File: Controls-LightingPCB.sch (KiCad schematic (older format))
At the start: 9 parts, among them J1 MinionConn, J3 Gecko_Cable, U1 LTC6820, U2 HX1188FNL

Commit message: Switched LEDs to back side and changed dimensions of board
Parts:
- removed J3: Gecko_Cable, UTSVT_Connectors:ribbon_cable_right_2x10, symbol Connector_Generic:Conn_02x10_Counter_Clockwise
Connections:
- net labels removed: UART-Tx, UART_Rx
- wire segments 77 -> 71
- no-connect marks 28 -> 14
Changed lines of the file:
@@
 Text Label 4350 4600 0    50   ~ 0
 IM
-Text Label 7150 4350 2    50   ~ 0
-UART-Tx
-Text Label 7150 4450 2    50   ~ 0
-UART_Rx
 $Sheet
 S 1750 1500 650  800
@@
 Wire Wire Line
 	2400 2200 2800 2200
-$Comp
-L Connector_Generic:Conn_02x10_Counter_Clockwise J3
-U 1 1 5F87CE03
-P 7800 4350
-F 0 "J3" H 7850 3625 50  0000 C CNN
-F 1 "Gecko_Cable" H 7850 3716 50  0000 C CNN
-F 2 "UTSVT_Connectors:ribbon_cable_right_2x10" H 7800 4350 50  0001 C CNN
-F 3 "~" H 7800 4350 50  0001 C CNN
-	1    7800 4350
-	-1   0    0    1
-$EndComp
-NoConn ~ 7500 3950
-NoConn ~ 7500 4050
-NoConn ~ 7500 4150
-NoConn ~ 7500 4250
-NoConn ~ 7500 4550
-NoConn ~ 7500 4650
-NoConn ~ 7500 4750
-NoConn ~ 8000 4650
-NoConn ~ 8000 4550
-NoConn ~ 8000 4450
-NoConn ~ 8000 4350
-NoConn ~ 8000 4250
-NoConn ~ 8000 4150
-NoConn ~ 8000 4050
-NoConn ~ 8000 3950
-NoConn ~ 8000 3850
-Wire Wire Line
-	7500 4450 6800 4450
-Wire Wire Line
-	6800 4350 7500 4350
-$Comp
-L power:GND #PWR0112
-U 1 1 5F8A761E
-P 8200 4850
-F 0 "#PWR0112" H 8200 4600 50  0001 C CNN
-F 1 "GND" H 8205 4677 50  0000 C CNN
-F 2 "" H 8200 4850 50  0001 C CNN
-F 3 "" H 8200 4850 50  0001 C CNN
-	1    8200 4850
-	-1   0    0    -1
-$EndComp
-$Comp
-L power:+3.3V #PWR0113
-U 1 1 5F8A7AF6
-P 7300 3750
-F 0 "#PWR0113" H 7300 3600 50  0001 C CNN
-F 1 "+3.3V" H 7315 3923 50  0000 C CNN
-F 2 "" H 7300 3750 50  0001 C CNN
-F 3 "" H 7300 3750 50  0001 C CNN
-	1    7300 3750
-	-1   0    0    -1
-$EndComp
-Wire Wire Line
-	7300 3750 7300 3850
-Wire Wire Line
-	7300 3850 7500 3850
-Wire Wire Line
-	8000 4750 8200 4750
-Wire Wire Line
-	8200 4750 8200 4850
 Wire Wire Line
 	6000 3350 6000 3450
@@
 Wire Wire Line
 	6000 3450 6100 3450
+NoConn ~ 6800 4350
+NoConn ~ 6800 4450
 $EndSCHEMATC

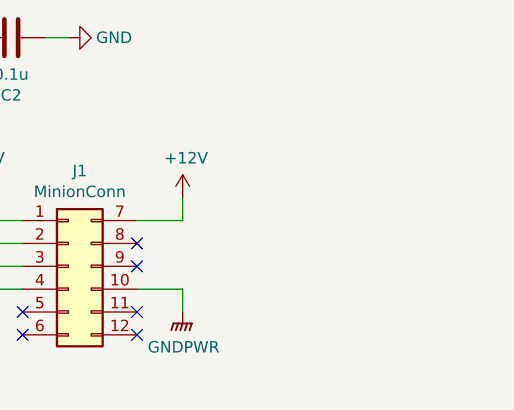
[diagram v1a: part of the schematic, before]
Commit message: Added mounting holes and adjusted design accordingly
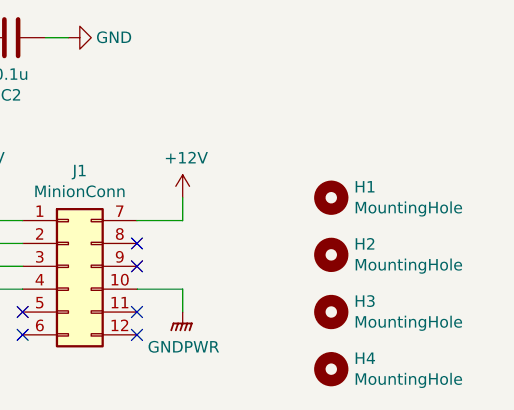
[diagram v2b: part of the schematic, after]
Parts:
- added H1, H2, H3, H4: MountingHole, MountingHole:MountingHole_3mm, symbol Mechanical:MountingHole
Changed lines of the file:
@@
 NoConn ~ 6800 4350
 NoConn ~ 6800 4450
+$Comp
+L Mechanical:MountingHole H4
+U 1 1 5F95A591
+P 7650 4900
+F 0 "H4" H 7750 4946 50  0000 L CNN
+F 1 "MountingHole" H 7750 4855 50  0000 L CNN
+F 2 "MountingHole:MountingHole_3mm" H 7650 4900 50  0001 C CNN
+F 3 "~" H 7650 4900 50  0001 C CNN
+	1    7650 4900
+	1    0    0    -1
+$EndComp
+$Comp
+L Mechanical:MountingHole H3
+U 1 1 5F95AB20
+P 7650 4650
+F 0 "H3" H 7750 4696 50  0000 L CNN
+F 1 "MountingHole" H 7750 4605 50  0000 L CNN
+F 2 "MountingHole:MountingHole_3mm" H 7650 4650 50  0001 C CNN
+F 3 "~" H 7650 4650 50  0001 C CNN
+	1    7650 4650
+	1    0    0    -1
+$EndComp
+$Comp
+L Mechanical:MountingHole H2
+U 1 1 5F95AF4E
+P 7650 4400
+F 0 "H2" H 7750 4446 50  0000 L CNN
+F 1 "MountingHole" H 7750 4355 50  0000 L CNN
+F 2 "MountingHole:MountingHole_3mm" H 7650 4400 50  0001 C CNN
+F 3 "~" H 7650 4400 50  0001 C CNN
+	1    7650 4400
+	1    0    0    -1
+$EndComp
+$Comp
+L Mechanical:MountingHole H1
+U 1 1 5F95B613
+P 7650 4150
+F 0 "H1" H 7750 4196 50  0000 L CNN
+F 1 "MountingHole" H 7750 4105 50  0000 L CNN
+F 2 "MountingHole:MountingHole_3mm" H 7650 4150 50  0001 C CNN
+F 3 "~" H 7650 4150 50  0001 C CNN
+	1    7650 4150
+	1    0    0    -1
+$EndComp
 $EndSCHEMATC

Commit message: Minor changes
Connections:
- net +3V3: no longer J1.1 (Pin_1)
- net GND: no longer J1.4 (Pin_4)
- no-connect marks 14 -> 16
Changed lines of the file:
@@
 $Descr A4 11693 8268
 encoding utf-8
-Sheet 1 4
+Sheet 1 5
 Title ""
 Date ""
@@
 $EndSheet
 Wire Wire Line
-	6100 4250 6300 4250
-Wire Wire Line
-	6100 4150 6100 4250
-Wire Wire Line
-	6100 4550 6300 4550
-Wire Wire Line
-	6100 4650 6100 4550
-$Comp
-L power:GND #PWR0101
-U 1 1 5F7E37DD
-P 6100 4650
-F 0 "#PWR0101" H 6100 4400 50  0001 C CNN
-F 1 "GND" H 6105 4477 50  0000 C CNN
-F 2 "" H 6100 4650 50  0001 C CNN
-F 3 "" H 6100 4650 50  0001 C CNN
-	1    6100 4650
-	1    0    0    -1
-$EndComp
-$Comp
-L power:+3.3V #PWR0102
-U 1 1 5F7E3562
-P 6100 4150
-F 0 "#PWR0102" H 6100 4000 50  0001 C CNN
-F 1 "+3.3V" H 6115 4323 50  0000 C CNN
-F 2 "" H 6100 4150 50  0001 C CNN
-F 3 "" H 6100 4150 50  0001 C CNN
-	1    6100 4150
-	1    0    0    -1
-$EndComp
-Wire Wire Line
 	7000 4250 7000 4150
 Wire Wire Line
@@
 	1    0    0    -1
 $EndComp
+$Comp
+L power:GND #PWR01
+U 1 1 5FA7B897
+P 3550 4250
+F 0 "#PWR01" H 3550 4000 50  0001 C CNN
+F 1 "GND" H 3555 4077 50  0000 C CNN
+F 2 "" H 3550 4250 50  0001 C CNN
+F 3 "" H 3550 4250 50  0001 C CNN
+	1    3550 4250
+	1    0    0    -1
+$EndComp
+NoConn ~ 6300 4550
+NoConn ~ 6300 4250
+$Sheet
+S 2700 3650 550  600
+U 5FA72DEA
+F0 "PowerDist" 50
+F1 "PowerDist.sch" 50
+F2 "GND" O R 3250 4150 50
+F3 "+5V" O R 3250 3850 50
+F4 "+3.3V" I R 3250 3950 50
+F5 "+12V" I R 3250 3750 50
+F6 "GNDPWR" I R 3250 4050 50
+$EndSheet
+$Comp
+L power:GNDPWR #PWR?
+U 1 1 5FA815F4
+P 3850 4250
+F 0 "#PWR?" H 3850 4050 50  0001 C CNN
+F 1 "GNDPWR" H 3854 4096 50  0000 C CNN
+F 2 "" H 3850 4200 50  0001 C CNN
+F 3 "" H 3850 4200 50  0001 C CNN
+	1    3850 4250
+	1    0    0    -1
+$EndComp
+$Comp
+L power:+3.3V #PWR?
+U 1 1 5FA8203D
+P 3900 3650
+F 0 "#PWR?" H 3900 3500 50  0001 C CNN
+F 1 "+3.3V" H 3915 3823 50  0000 C CNN
+F 2 "" H 3900 3650 50  0001 C CNN
+F 3 "" H 3900 3650 50  0001 C CNN
+	1    3900 3650
+	1    0    0    -1
+$EndComp
+$Comp
+L power:+5V #PWR?
+U 1 1 5FA82F89
+P 3700 3650
+F 0 "#PWR?" H 3700 3500 50  0001 C CNN
+F 1 "+5V" H 3715 3823 50  0000 C CNN
+F 2 "" H 3700 3650 50  0001 C CNN
+F 3 "" H 3700 3650 50  0001 C CNN
+	1    3700 3650
+	1    0    0    -1
+$EndComp
+$Comp
+L power:+12V #PWR?
+U 1 1 5FA838E6
+P 3500 3650
+F 0 "#PWR?" H 3500 3500 50  0001 C CNN
+F 1 "+12V" H 3515 3823 50  0000 C CNN
+F 2 "" H 3500 3650 50  0001 C CNN
+F 3 "" H 3500 3650 50  0001 C CNN
+	1    3500 3650
+	1    0    0    -1
+$EndComp
+Wire Wire Line
+	3250 4150 3550 4150
+Wire Wire Line
+	3550 4150 3550 4250
+Wire Wire Line
+	3250 4050 3850 4050
+Wire Wire Line
+	3850 4050 3850 4250
+Wire Wire Line
+	3250 3950 3900 3950
+Wire Wire Line
+	3900 3950 3900 3650
+Wire Wire Line
+	3250 3850 3700 3850
+Wire Wire Line
+	3700 3850 3700 3650
+Wire Wire Line
+	3250 3750 3500 3750
+Wire Wire Line
+	3500 3750 3500 3650
 $EndSCHEMATC

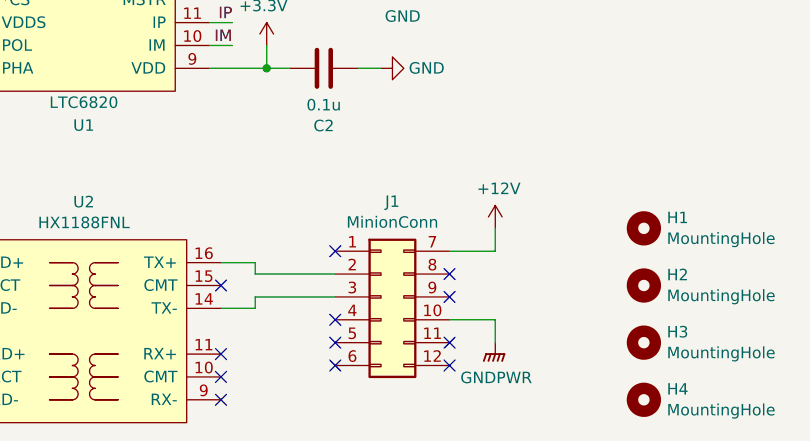
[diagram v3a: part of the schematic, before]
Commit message: Changed all switch connectors to horizontal, board dimensions to 2.5in by 4.5in, and started board layout
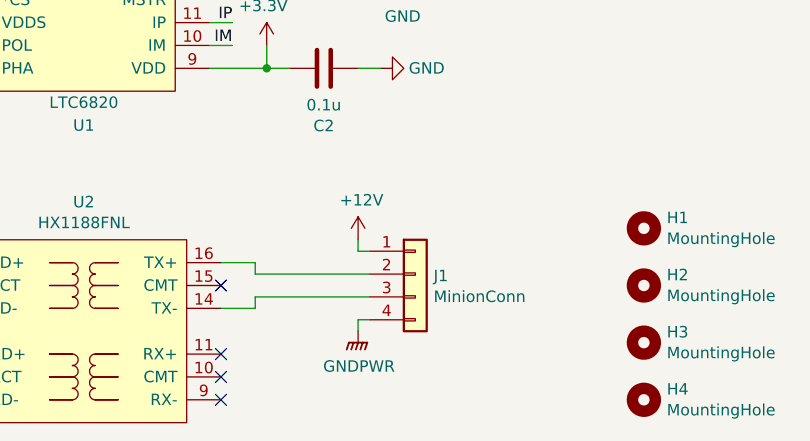
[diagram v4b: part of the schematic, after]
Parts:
- removed J1: MinionConn, UTSVT_Connectors:Molex_MicroFit3.0_2x6xP3.00mm_PolarizingPeg_Vertical, symbol Connector_Generic:Conn_02x06_Top_Bottom
- added J1: MinionConn, Connector_Molex:Molex_Micro-Fit_3.0_43650-0400_1x04_P3.00mm_Horizontal, symbol Connector_Generic:Conn_01x04
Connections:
- net +12V: now also J1.1 (Pin_1)
- net GNDPWR: now also J1.4 (Pin_4)
- net at U2.16 (TX+): now also J1.2 (Pin_2)
- net at U2.14 (TX-): now also J1.3 (Pin_3)
- no-connect marks 16 -> 8
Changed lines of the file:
@@
 F21 "MOSI" O R 4050 2850 50
 $EndSheet
-Wire Wire Line
-	7000 4250 7000 4150
-Wire Wire Line
-	6800 4250 7000 4250
-Wire Wire Line
-	7000 4550 7000 4650
-Wire Wire Line
-	6800 4550 7000 4550
-NoConn ~ 6300 4750
-NoConn ~ 6300 4650
-NoConn ~ 6800 4750
-NoConn ~ 6800 4650
 $Comp
 L power:GNDPWR #PWR0103
 U 1 1 5F7E16B8
-P 7000 4650
-F 0 "#PWR0103" H 7000 4450 50  0001 C CNN
-F 1 "GNDPWR" H 7004 4496 50  0000 C CNN
-F 2 "" H 7000 4600 50  0001 C CNN
-F 3 "" H 7000 4600 50  0001 C CNN
-	1    7000 4650
+P 6400 4600
+F 0 "#PWR0103" H 6400 4400 50  0001 C CNN
+F 1 "GNDPWR" H 6404 4446 50  0000 C CNN
+F 2 "" H 6400 4550 50  0001 C CNN
+F 3 "" H 6400 4550 50  0001 C CNN
+	1    6400 4600
 	1    0    0    -1
 $EndComp
@@
 L power:+12V #PWR0104
 U 1 1 5F7E142C
-P 7000 4150
-F 0 "#PWR0104" H 7000 4000 50  0001 C CNN
-F 1 "+12V" H 7015 4323 50  0000 C CNN
-F 2 "" H 7000 4150 50  0001 C CNN
-F 3 "" H 7000 4150 50  0001 C CNN
-	1    7000 4150
-	1    0    0    -1
-$EndComp
-$Comp
-L Connector_Generic:Conn_02x06_Top_Bottom J1
-U 1 1 5F7DD986
-P 6500 4450
-F 0 "J1" H 6550 4867 50  0000 C CNN
-F 1 "MinionConn" H 6550 4776 50  0000 C CNN
-F 2 "UTSVT_Connectors:Molex_MicroFit3.0_2x6xP3.00mm_PolarizingPeg_Vertical" H 6500 4450 50  0001 C CNN
-F 3 "~" H 6500 4450 50  0001 C CNN
-	1    6500 4450
+P 6400 4200
+F 0 "#PWR0104" H 6400 4050 50  0001 C CNN
+F 1 "+12V" H 6415 4373 50  0000 C CNN
+F 2 "" H 6400 4200 50  0001 C CNN
+F 3 "" H 6400 4200 50  0001 C CNN
+	1    6400 4200
 	1    0    0    -1
 $EndComp
@@
 	5950 4300 5950 4350
 Wire Wire Line
-	5950 4350 6300 4350
-Wire Wire Line
 	5800 4500 5950 4500
 Wire Wire Line
 	5950 4500 5950 4450
-Wire Wire Line
-	5950 4450 6300 4450
 NoConn ~ 5800 4400
 NoConn ~ 5800 4700
@@
 Wire Wire Line
 	6000 3450 6100 3450
-NoConn ~ 6800 4350
-NoConn ~ 6800 4450
 $Comp
 L Mechanical:MountingHole H4
@@
 	1    0    0    -1
 $EndComp
-NoConn ~ 6300 4550
-NoConn ~ 6300 4250
 $Sheet
 S 2700 3650 550  600
@@
 $EndSheet
 $Comp
-L power:GNDPWR #PWR?
+L power:GNDPWR #PWR0101
 U 1 1 5FA815F4
 P 3850 4250
-F 0 "#PWR?" H 3850 4050 50  0001 C CNN
+F 0 "#PWR0101" H 3850 4050 50  0001 C CNN
 F 1 "GNDPWR" H 3854 4096 50  0000 C CNN
 F 2 "" H 3850 4200 50  0001 C CNN
@@
 $EndComp
 $Comp
-L power:+3.3V #PWR?
+L power:+3.3V #PWR0102
 U 1 1 5FA8203D
 P 3900 3650
-F 0 "#PWR?" H 3900 3500 50  0001 C CNN
+F 0 "#PWR0102" H 3900 3500 50  0001 C CNN
 F 1 "+3.3V" H 3915 3823 50  0000 C CNN
 F 2 "" H 3900 3650 50  0001 C CNN
@@
 $EndComp
 $Comp
-L power:+5V #PWR?
+L power:+5V #PWR0112
 U 1 1 5FA82F89
 P 3700 3650
-F 0 "#PWR?" H 3700 3500 50  0001 C CNN
+F 0 "#PWR0112" H 3700 3500 50  0001 C CNN
 F 1 "+5V" H 3715 3823 50  0000 C CNN
 F 2 "" H 3700 3650 50  0001 C CNN
@@
 $EndComp
 $Comp
-L power:+12V #PWR?
+L power:+12V #PWR0113
 U 1 1 5FA838E6
 P 3500 3650
-F 0 "#PWR?" H 3500 3500 50  0001 C CNN
+F 0 "#PWR0113" H 3500 3500 50  0001 C CNN
 F 1 "+12V" H 3515 3823 50  0000 C CNN
 F 2 "" H 3500 3650 50  0001 C CNN
@@
 Wire Wire Line
 	3500 3750 3500 3650
+$Comp
+L Connector_Generic:Conn_01x04 J1
+U 1 1 5FBD3314
+P 6650 4350
+F 0 "J1" H 6730 4342 50  0000 L CNN
+F 1 "MinionConn" H 6730 4251 50  0000 L CNN
+F 2 "Connector_Molex:Molex_Micro-Fit_3.0_43650-0400_1x04_P3.00mm_Horizontal" H 6650 4350 50  0001 C CNN
+F 3 "~" H 6650 4350 50  0001 C CNN
+	1    6650 4350
+	1    0    0    -1
+$EndComp
+Wire Wire Line
+	6400 4200 6400 4250
+Wire Wire Line
+	6400 4250 6450 4250
+Wire Wire Line
+	6450 4550 6400 4550
+Wire Wire Line
+	6400 4550 6400 4600
+Wire Wire Line
+	5950 4350 6450 4350
+Wire Wire Line
+	5950 4450 6450 4450
 $EndSCHEMATC

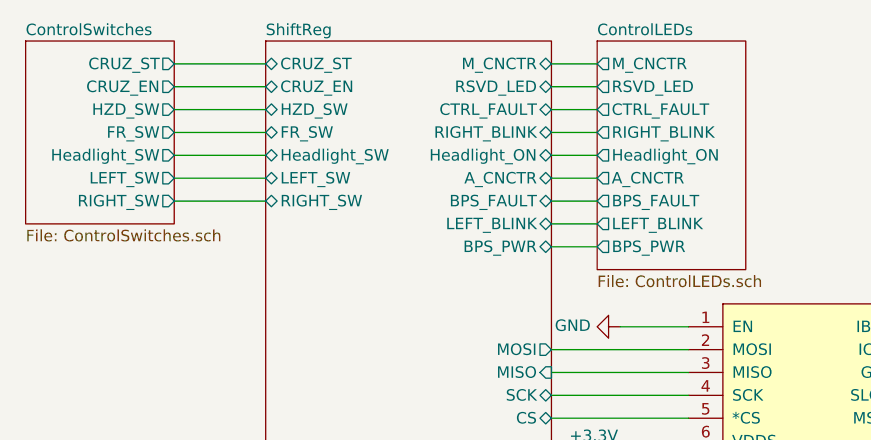
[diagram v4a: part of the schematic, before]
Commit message: Added Regen switch, deleted RSVD LED
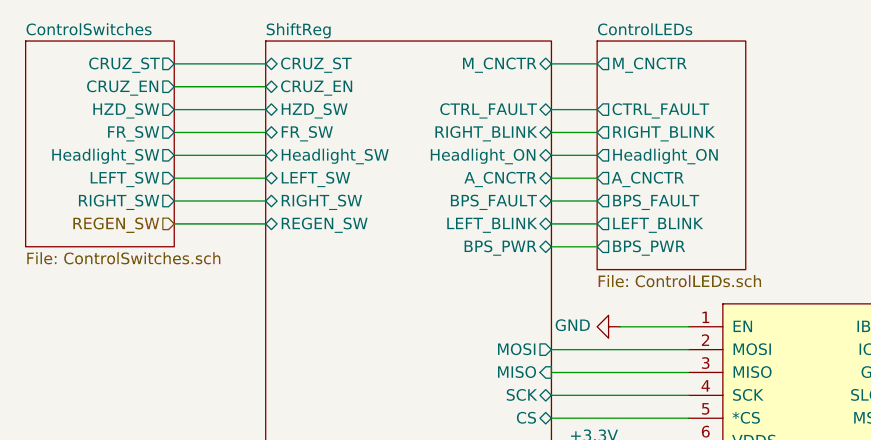
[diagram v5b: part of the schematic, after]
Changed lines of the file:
@@
 	4250 1800 4050 1800
-Wire Wire Line
-	4050 1700 4250 1700
 Wire Wire Line
 	4250 1600 4050 1600
@@
 F1 "ControlLEDs.sch" 50
 F2 "M_CNCTR" O L 4250 1600 50
-F3 "RSVD_LED" O L 4250 1700 50
-F4 "A_CNCTR" O L 4250 2100 50
-F5 "CTRL_FAULT" O L 4250 1800 50
-F6 "RIGHT_BLINK" O L 4250 1900 50
-F7 "Headlight_ON" O L 4250 2000 50
-F8 "BPS_FAULT" O L 4250 2200 50
-F9 "LEFT_BLINK" O L 4250 2300 50
-F10 "BPS_PWR" O L 4250 2400 50
+F3 "A_CNCTR" O L 4250 2100 50
+F4 "CTRL_FAULT" O L 4250 1800 50
+F5 "RIGHT_BLINK" O L 4250 1900 50
+F6 "Headlight_ON" O L 4250 2000 50
+F7 "BPS_FAULT" O L 4250 2200 50
+F8 "LEFT_BLINK" O L 4250 2300 50
+F9 "BPS_PWR" O L 4250 2400 50
 $EndSheet
 $Sheet
@@
 F1 "ShiftReg.sch" 50
 F2 "M_CNCTR" B R 4050 1600 50
-F3 "RSVD_LED" B R 4050 1700 50
-F4 "CTRL_FAULT" B R 4050 1800 50
-F5 "RIGHT_BLINK" B R 4050 1900 50
-F6 "Headlight_ON" B R 4050 2000 50
-F7 "A_CNCTR" B R 4050 2100 50
-F8 "BPS_FAULT" B R 4050 2200 50
-F9 "LEFT_BLINK" B R 4050 2300 50
-F10 "BPS_PWR" B R 4050 2400 50
-F11 "CRUZ_ST" B L 2800 1600 50
-F12 "CRUZ_EN" B L 2800 1700 50
-F13 "HZD_SW" B L 2800 1800 50
-F14 "FR_SW" B L 2800 1900 50
-F15 "Headlight_SW" B L 2800 2000 50
-F16 "LEFT_SW" B L 2800 2100 50
-F17 "RIGHT_SW" B L 2800 2200 50
-F18 "CS" B R 4050 3150 50
-F19 "SCK" B R 4050 3050 50
-F20 "MISO" I R 4050 2950 50
-F21 "MOSI" O R 4050 2850 50
+F3 "CTRL_FAULT" B R 4050 1800 50
+F4 "RIGHT_BLINK" B R 4050 1900 50
+F5 "Headlight_ON" B R 4050 2000 50
+F6 "A_CNCTR" B R 4050 2100 50
+F7 "BPS_FAULT" B R 4050 2200 50
+F8 "LEFT_BLINK" B R 4050 2300 50
+F9 "BPS_PWR" B R 4050 2400 50
+F10 "CRUZ_ST" B L 2800 1600 50
+F11 "CRUZ_EN" B L 2800 1700 50
+F12 "HZD_SW" B L 2800 1800 50
+F13 "FR_SW" B L 2800 1900 50
+F14 "Headlight_SW" B L 2800 2000 50
+F15 "LEFT_SW" B L 2800 2100 50
+F16 "RIGHT_SW" B L 2800 2200 50
+F17 "CS" B R 4050 3150 50
+F18 "SCK" B R 4050 3050 50
+F19 "MISO" I R 4050 2950 50
+F20 "MOSI" O R 4050 2850 50
+F21 "REGEN_SW" B L 2800 2300 50
 $EndSheet
 $Comp
@@
 IM
 $Sheet
-S 1750 1500 650  800
+S 1750 1500 650  900
 U 5F78B3EB
 F0 "ControlSwitches" 50
@@
 Wire Wire Line
 	5950 4450 6450 4450
+Text HLabel 2400 2300 0    50   Input ~ 0
+REGEN_SW
+Wire Wire Line
+	2400 2300 2800 2300
 $EndSCHEMATC

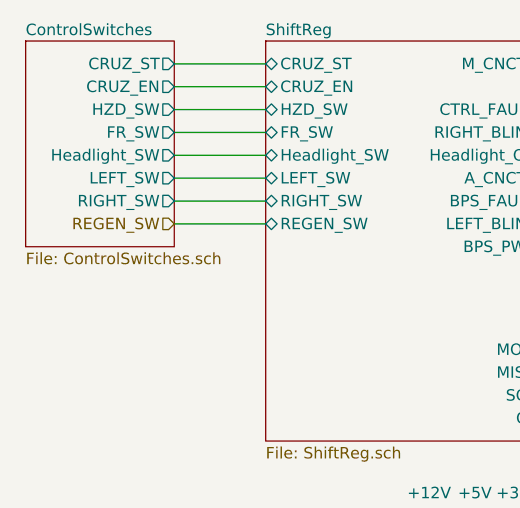
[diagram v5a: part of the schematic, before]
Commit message: Started placing routes, did not finish
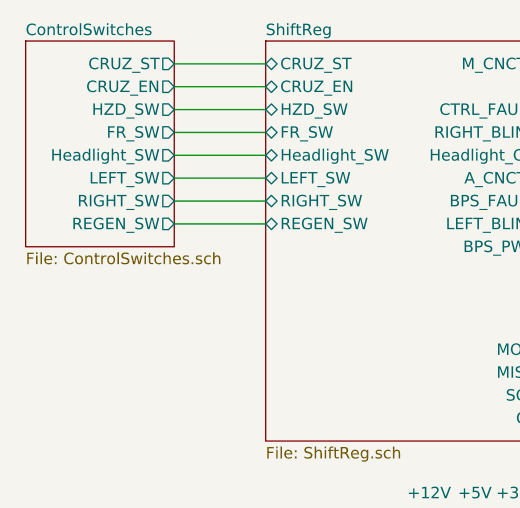
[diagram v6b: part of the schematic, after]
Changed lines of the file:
@@
 F7 "LEFT_SW" O R 2400 2100 50
 F8 "RIGHT_SW" O R 2400 2200 50
+F9 "REGEN_SW" O R 2400 2300 50
 $EndSheet
 Wire Wire Line
@@
 Wire Wire Line
 	5950 4450 6450 4450
-Text HLabel 2400 2300 0    50   Input ~ 0
-REGEN_SW
 Wire Wire Line
 	2400 2300 2800 2300

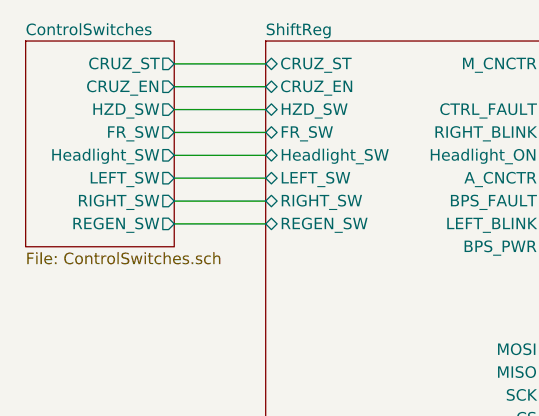
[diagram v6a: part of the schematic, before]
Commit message: Finished connections and changed F/W switch, but hierarchial labels on schematic need to be fixed
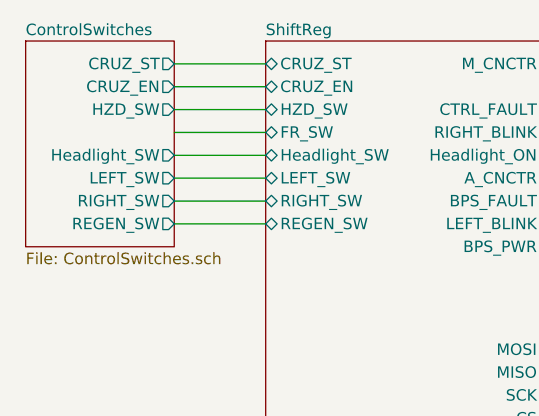
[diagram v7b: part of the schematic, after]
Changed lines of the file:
@@
 F3 "CRUZ_EN" O R 2400 1700 50
 F4 "HZD_SW" O R 2400 1800 50
-F5 "FR_SW" O R 2400 1900 50
-F6 "Headlight_SW" O R 2400 2000 50
-F7 "LEFT_SW" O R 2400 2100 50
-F8 "RIGHT_SW" O R 2400 2200 50
-F9 "REGEN_SW" O R 2400 2300 50
+F5 "Headlight_SW" O R 2400 2000 50
+F6 "LEFT_SW" O R 2400 2100 50
+F7 "RIGHT_SW" O R 2400 2200 50
+F8 "REGEN_SW" O R 2400 2300 50
 $EndSheet
 Wire Wire Line
